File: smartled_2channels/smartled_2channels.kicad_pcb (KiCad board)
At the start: 2 copper layers, 83 x 16 mm, 89 parts, among them J2 Conn_01x02, Q1 Q_NMOS_GSD, SW1 SW_Push, U1 OC5028B, U2 MAX485E, U3 PY32F003F1xUx, U4 OC5864, U5 SGM2033-3.3, U6 OC5028B, U7 GS8521

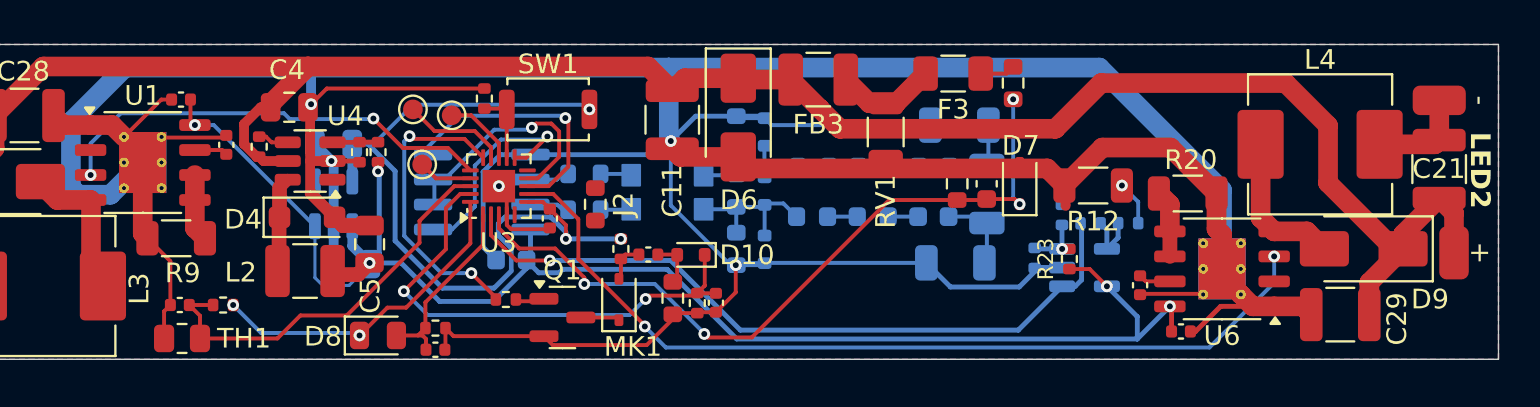
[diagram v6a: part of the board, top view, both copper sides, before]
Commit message: 修复一些DRC错误，优化布线
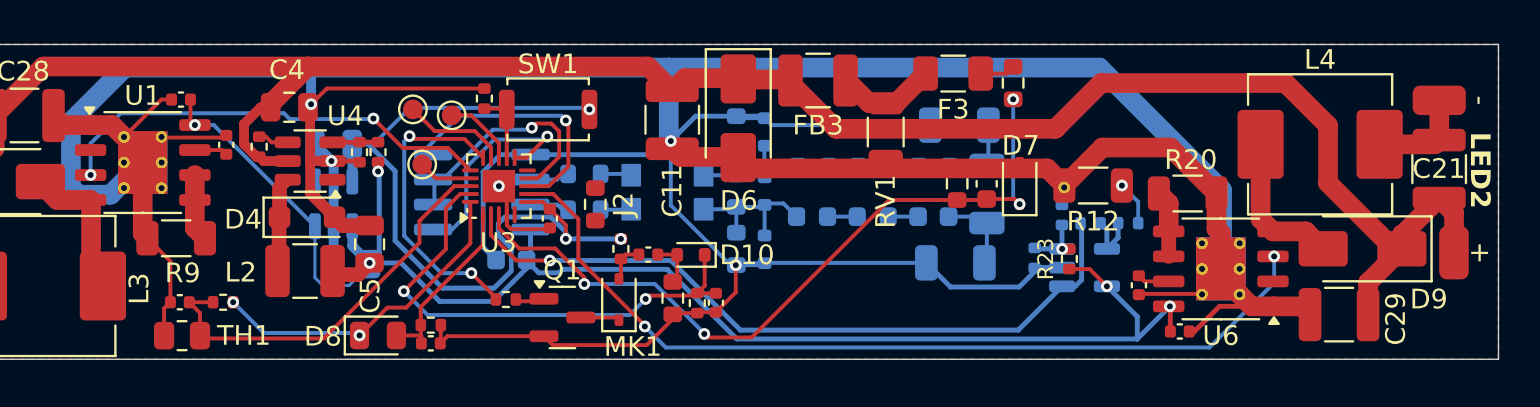
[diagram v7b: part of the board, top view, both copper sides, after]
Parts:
- NT1: footprint NetTie:NetTie-2_SMD_Pad0.5mm -> project_footprints:NetTie-2_VIA_Pad0.6_0.3mm
- U1, U6: footprint Package_SO:HSOP-8-1EP_3.9x4.9mm_P1.27mm_EP2.41x3.1mm_ThermalVias -> project_footprints:HSOP-8-1EP_3.9x4.9mm_P1.27mm_EP2.41x3.1mm_ThermalVias_0.3_0.6mm
- moved NT1 0.44 mm to (168.3, 93.4)
- moved C18 0.40 mm to (136.1, 101.3)
- moved R14 0.28 mm to (136.1, 100.4)
- moved C17 0.14 mm to (123.4, 99.2)
- moved R15 0.14 mm to (125.6, 99.2)
- moved TH1 0.14 mm to (123.5, 100.9)
- moved C19 0.06 mm to (172.1, 98.3)
- moved C29 0.06 mm to (182.3, 99.8)
- moved D9 0.06 mm to (183.5, 96.5)
- moved U6 0.06 mm to (176.3, 97.5)
- moved C20 0.06 mm to (174.2, 100.7)
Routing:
- net /Isamp+: track 0.00 -> 0.93 mm

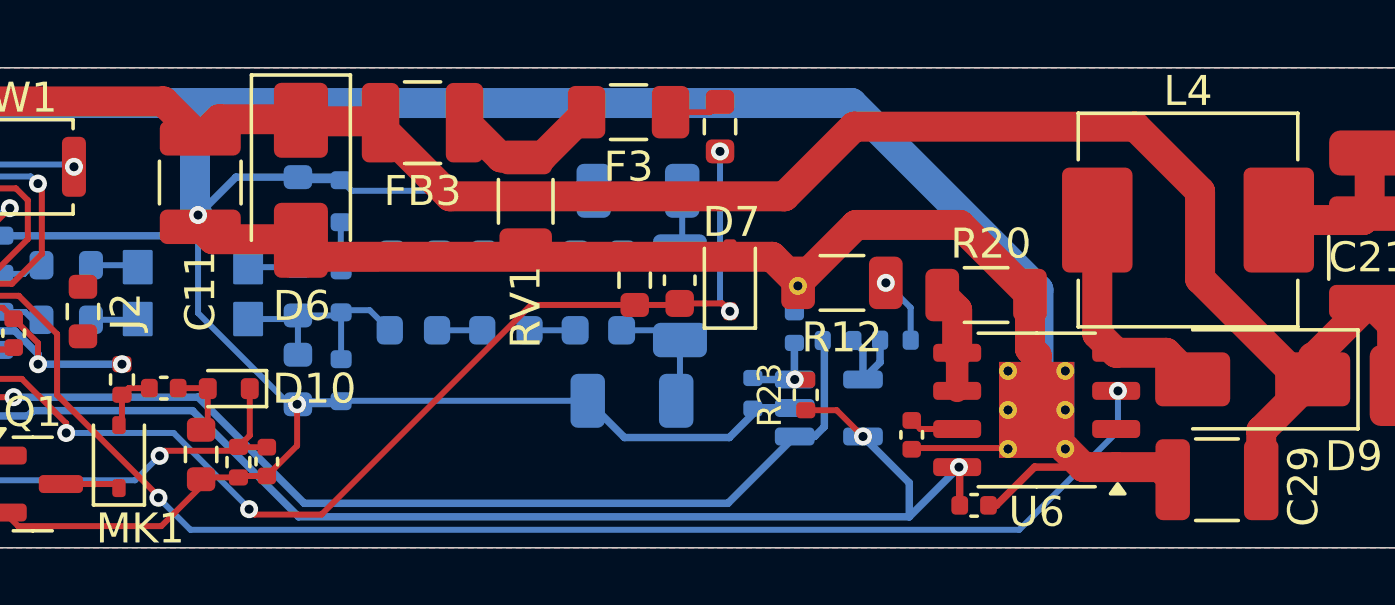
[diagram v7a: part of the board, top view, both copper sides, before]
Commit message: 电源和通信端口放置通孔焊盘用于焊接电线
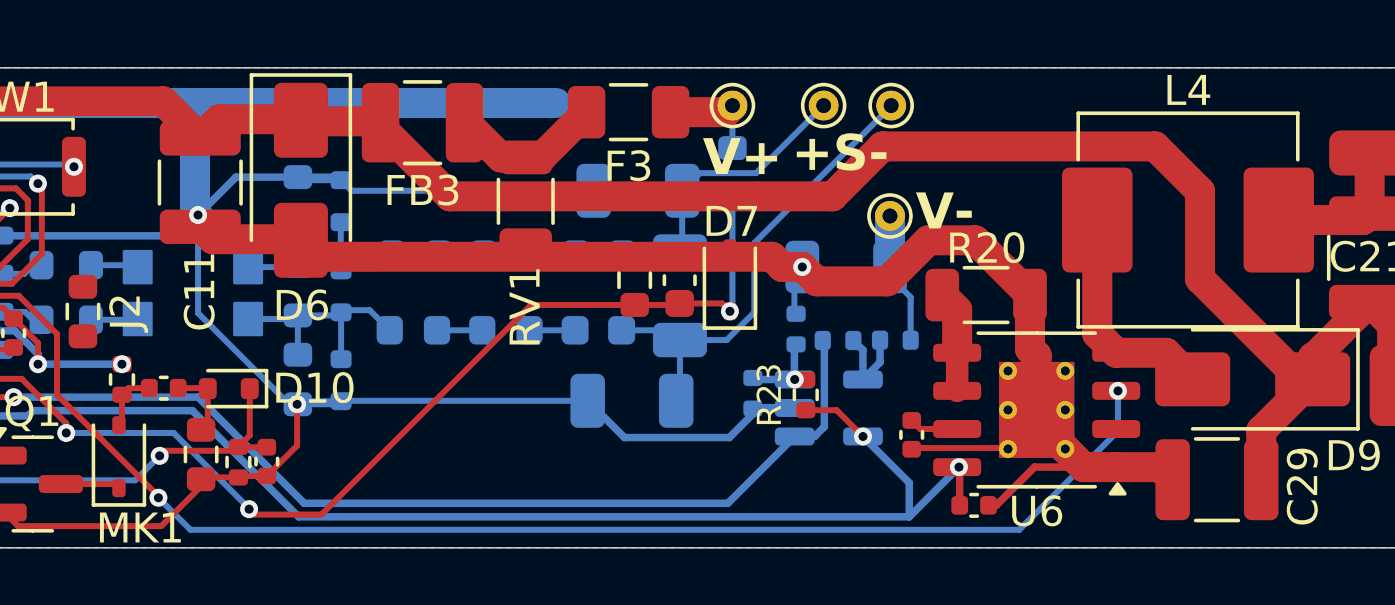
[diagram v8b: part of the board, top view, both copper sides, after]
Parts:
- removed NT1: NetTie_2, project_footprints:NetTie-2_VIA_Pad0.6_0.3mm
- added TP4: V+, TestPoint:TestPoint_THTPad_D1.0mm_Drill0.5mm, F.Cu at (166.2, 87.4)
- added TP5: V-, TestPoint:TestPoint_THTPad_D1.0mm_Drill0.5mm, F.Cu at (171.4, 91.0)
- added TP6: S-, TestPoint:TestPoint_THTPad_D1.0mm_Drill0.5mm, F.Cu at (171.4, 87.4)
- added TP7: S+, TestPoint:TestPoint_THTPad_D1.0mm_Drill0.5mm, F.Cu at (169.2, 87.4)
- R10, R12: moved to B.Cu
- moved R10 1.59 mm to (166.2, 89.6)
- moved R12 0.55 mm to (169.9, 92.7)
- moved R16 0.07 mm to (168.3, 94.8)
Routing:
- net GND: track 259.7 -> 236.6 mm, vias 5 -> 6
- net /485-: track 4.16 -> 15.9 mm
- net /485+: track 4.01 -> 9.91 mm
- net /VIN-: track 2.25 -> 4.43 mm, vias 1 -> 0
- net /VIN+: track 1.79 -> 3.66 mm
- net /ADC_V: track 38.1 -> 36.5 mm, vias 4 -> 3
- net VINP: track 109.8 -> 109.2 mm
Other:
- board text added: "+S-"
- board text added: "-S+"
- board text added: "In DC 6-100V Out 1.5Amax/CH"
- board text added: "V+"
- board text added: "V-"
